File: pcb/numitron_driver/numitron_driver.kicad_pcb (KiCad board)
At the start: 2 copper layers, 30.4 x 28 mm, 6 parts, among them J0 Conn_02x04_Male, J1 IV-9, U0 TPIC6595

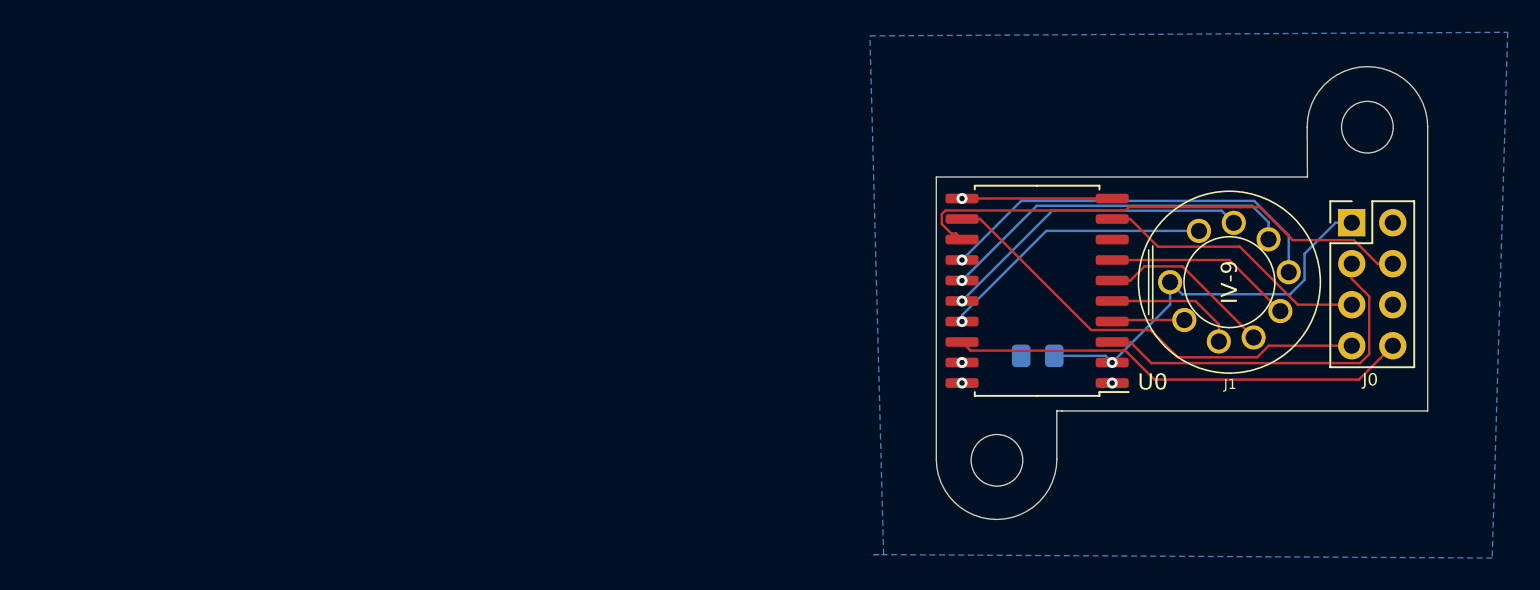
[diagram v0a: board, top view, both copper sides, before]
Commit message: driver and basic shiftout test code for the tube driver
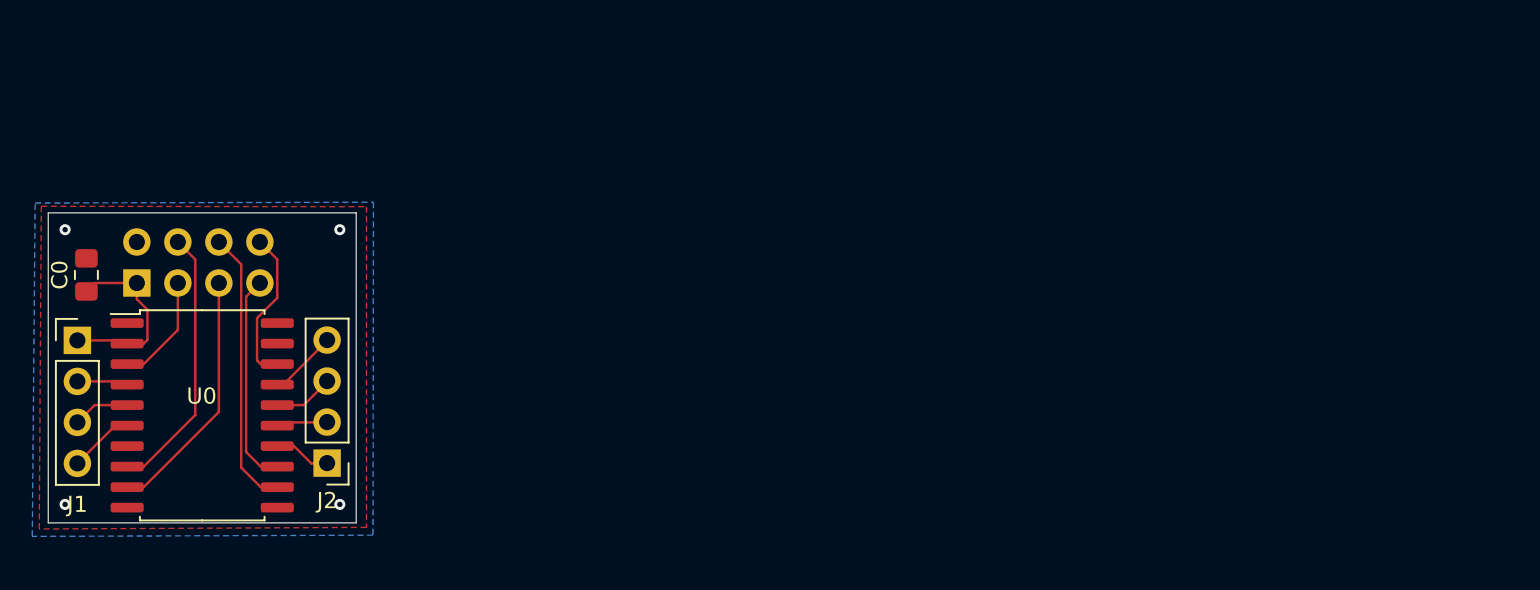
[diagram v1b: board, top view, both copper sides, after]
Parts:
- removed REF** (x2): MountingHole_3.2mm_M3, MountingHole:MountingHole_3.2mm_M3
- added J2: Conn_01x04_Female, Connector_PinHeader_2.54mm:PinHeader_1x04_P2.54mm_Vertical, F.Cu at (103.6, 111.0)
- C0: moved to F.Cu
- J0: value Conn_02x04_Male -> Conn_02x04_Odd_Even; footprint Connector_PinHeader_2.54mm:PinHeader_2x04_P2.54mm_Vertical -> Connector_PinSocket_2.54mm:PinSocket_2x04_P2.54mm_Vertical; moved to B.Cu
- J1: value IV-9 -> Conn_01x04_Female; footprint numitron_clock:NUM_IV-9 -> Connector_PinHeader_2.54mm:PinHeader_1x04_P2.54mm_Vertical
- moved J0 75.4 mm to (91.8, 99.8), turned to 270 degrees
- moved J1 71.5 mm to (88.1, 103.4), turned to 0 degrees
- moved C0 59.1 mm to (88.7, 99.3), turned to 90 degrees
- moved U0 52.3 mm to (95.9, 108.0), turned to 0 degrees
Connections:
- U0 pad 12: Net-(J0-Pad7) -> Net-(J0-Pad6)
- U0 pad 13: Net-(J0-Pad4) -> Net-(J0-Pad7)
- U0 pad 14: Net-(J1-Pad6) -> Net-(J2-Pad1)
- U0 pad 15: Net-(J1-Pad7) -> Net-(J2-Pad2)
- U0 pad 16: Net-(J1-Pad8) -> Net-(J2-Pad3)
- U0 pad 17: Net-(J1-Pad9) -> Net-(J2-Pad4)
- U0 pad 7: Net-(J1-Pad5) -> Net-(U0-Pad7)
- U0 pad 8: Net-(J0-Pad6) -> Net-(J0-Pad4)
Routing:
- net Net-(J1-Pad6): track 24.9 -> 0.00 mm, vias 1 -> 0
- net Net-(J1-Pad7): track 22.4 -> 0.00 mm, vias 1 -> 0
- net Net-(J1-Pad8): track 19.5 -> 0.00 mm, vias 1 -> 0
- net Net-(J0-Pad8): track 28.5 -> 9.65 mm
- net Net-(J0-Pad6): track 0.00 -> 17.3 mm
- net Net-(J1-Pad9): track 17.2 -> 0.00 mm, vias 1 -> 0
- net Net-(J0-Pad3): track 22.7 -> 6.93 mm
- net Net-(J0-Pad4): track 31.8 -> 16.7 mm
- net Net-(J0-Pad7): track 28.0 -> 13.1 mm
- net Net-(C0-Pad1): track 24.6 -> 11.7 mm, vias 1 -> 0
- net Net-(J1-Pad5): track 11.7 -> 0.00 mm
- net GND: track 9.30 -> 0.00 mm
- net Net-(J1-Pad4): track 10.9 -> 4.05 mm
- net Net-(J1-Pad3): track 8.27 -> 3.53 mm
- net Net-(J2-Pad4): track 0.00 -> 4.25 mm
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- added copper zone on F.Cu, net GND
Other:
- board size 30.4 x 28 mm -> 19.1 x 19.2 mm
